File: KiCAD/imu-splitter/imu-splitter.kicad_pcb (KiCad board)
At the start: 4 copper layers, 54 x 54 mm, 11 parts, among them J1 4P4C, J2 4P4C, J3 4P4C, J4 4P4C, J5 4P4C, J6 4P4C, J7 Conn_02x13_Odd_Even, J8 Conn_01x04, U1 AZ1117-3.3

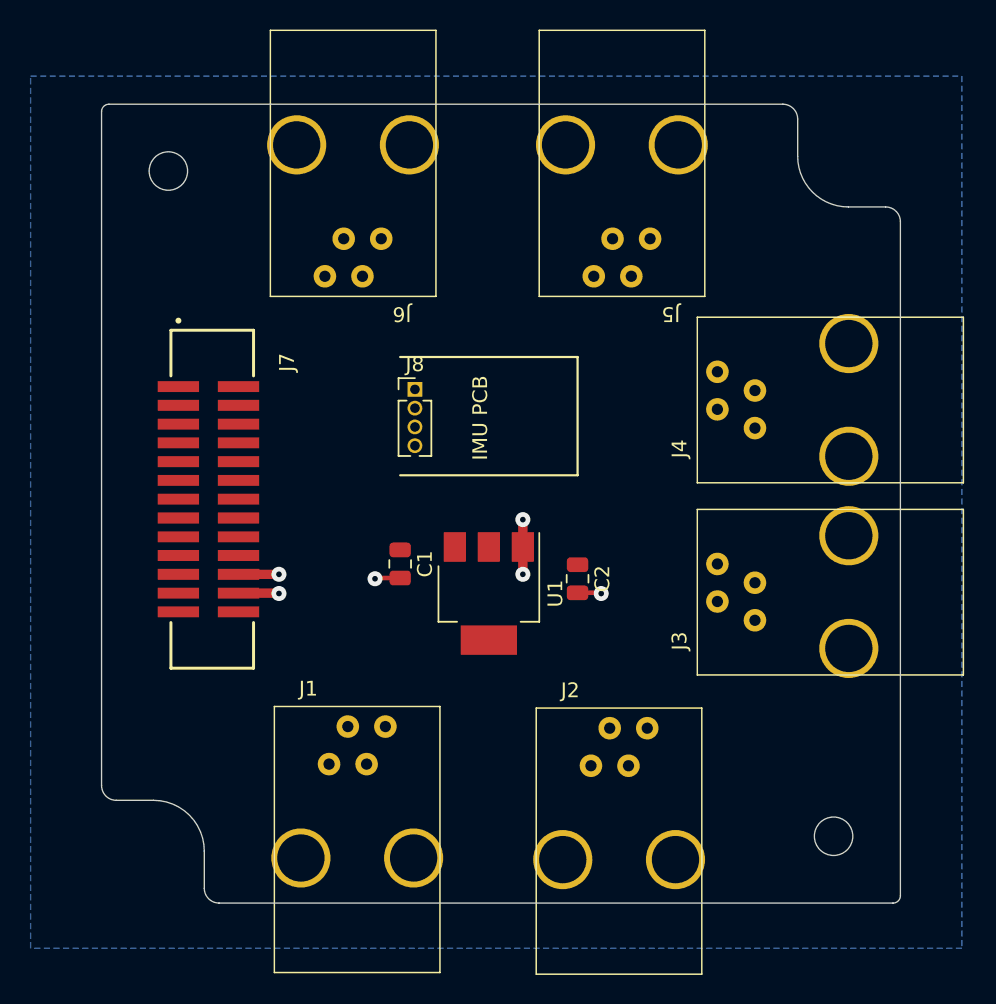
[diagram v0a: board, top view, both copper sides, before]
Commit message: tentative placement of splitter
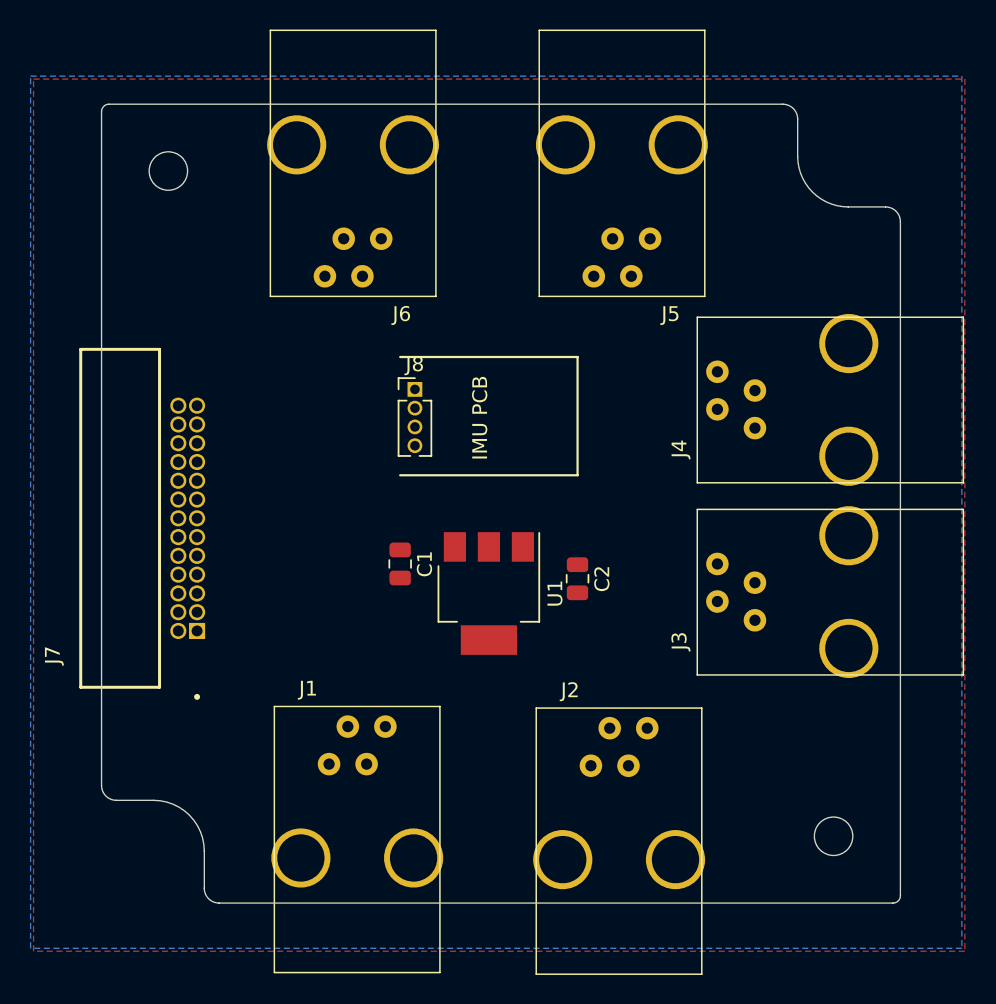
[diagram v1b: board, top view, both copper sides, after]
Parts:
- J7: value Conn_02x13_Odd_Even -> SHF-113-01-L-D-SM; footprint models:SAMTEC_SHF-113-01-L-D-SM -> models:SAMTEC_SHF-113-01-L-D-RA
- moved J7 1.91 mm to (169.6, 102.9), turned to 90 degrees
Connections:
- J2 pad 2: /TX1 -> /RX1
- J2 pad 3: /RX1 -> /TX1
- J7 pad 10: /RX2 -> /TX6
- J7 pad 11: /TX3 -> /TX1
- J7 pad 12: /RX3 -> /RX6
- J7 pad 13: /TX4 -> /RX1
- J7 pad 15: /TX5 -> /TX2
- J7 pad 16: /RX5 -> /TX4
- J7 pad 17: /TX6 -> /RX2
- J7 pad 18: /RX6 -> /RX3
- J7 pad 20: unconnected-(J7-Pin_20-Pad20) -> /TX3
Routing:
- net GND: track 12.5 -> 0.00 mm, vias 6 -> 0
- added copper zone on F.Cu, net +3.3V

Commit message: updates before v1 fab
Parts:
- added D1: LED, LED_SMD:LED_0805_2012Metric_Pad1.15x1.40mm_HandSolder, F.Cu at (183.4, 109.6)
- added D2: LED, LED_SMD:LED_0805_2012Metric_Pad1.15x1.40mm_HandSolder, F.Cu at (197.3, 109.6)
- added J9: Conn_01x05, Connector_PinHeader_2.54mm:PinHeader_1x05_P2.54mm_Vertical, F.Cu at (178.4, 110.1)
- added R1: 1.5k, Resistor_SMD:R_0805_2012Metric_Pad1.20x1.40mm_HandSolder, F.Cu at (182.2, 105.5)
- added R2: 510, Capacitor_SMD:C_0805_2012Metric_Pad1.18x1.45mm_HandSolder, F.Cu at (198.7, 105.6)
- C1, C2: footprint Capacitor_SMD:C_0805_2012Metric -> Capacitor_SMD:C_0805_2012Metric_Pad1.18x1.45mm_HandSolder
- moved C2 1.33 mm to (196.0, 105.7)
- moved C1 0.91 mm to (184.8, 105.5)
- moved J3 0.64 mm to (208.1, 110.4)
- moved J4 0.12 mm to (208.1, 96.8)
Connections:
- J7 pad 10: /TX6 -> /TX1
- J7 pad 11: /TX1 -> /RX6
- J7 pad 12: /RX6 -> /RX1
- J7 pad 13: /RX1 -> /TX6
- J7 pad 14: /RX4 -> /RX0
- J7 pad 15: /TX2 -> /TX4
- J7 pad 16: /TX4 -> /TX0
- J7 pad 17: /RX2 -> /RX4
- J7 pad 18: /RX3 -> unconnected-(J7-Pin_18-Pad18)
- J7 pad 19: unconnected-(J7-Pin_19-Pad19) -> /TX5
- J7 pad 20: /TX3 -> unconnected-(J7-Pin_20-Pad20)
- J7 pad 21: unconnected-(J7-Pin_21-Pad21) -> /RX5
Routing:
- net /RX0: track 0.00 -> 54.2 mm
- net /RX2: track 0.00 -> 48.9 mm
- net /TX2: track 0.00 -> 46.3 mm
- net /TX1: track 0.00 -> 45.6 mm
- net /TX0: track 0.00 -> 45.4 mm
- net /RX1: track 0.00 -> 43.0 mm
- net /RX3: track 0.00 -> 43.0 mm
- net /TX3: track 0.00 -> 40.0 mm
- net /TX4: track 0.00 -> 36.6 mm
- net /RX4: track 0.00 -> 34.9 mm
- net +5V: track 0.00 -> 23.0 mm
- net /RX5: track 0.00 -> 19.6 mm
- net /RX6: track 0.00 -> 17.9 mm
- net /TX6: track 0.00 -> 17.8 mm
- net /TX5: track 0.00 -> 17.2 mm
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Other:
- copper layers 4 -> 2
- board text added: "2024-01 E. Hazen"
- board text added: "3.3"
- board text added: "5.0"
- board text added: "DOSI IMU Splitter V1.0"
- board text added: "GND"
- board text added: "K"
- board text added: "RX0"
- board text added: "TX0"

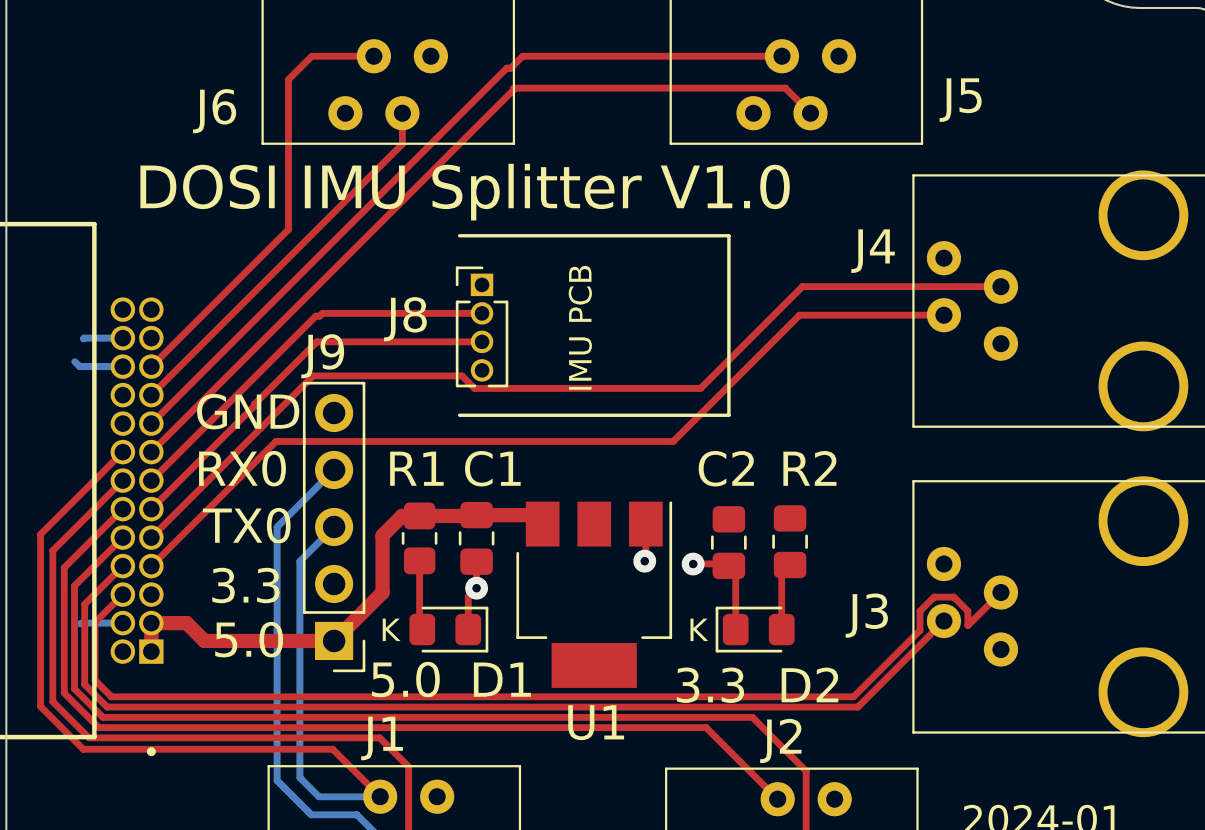
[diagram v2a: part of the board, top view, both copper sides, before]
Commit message: fix silkscreen and move IMU PCB a bit
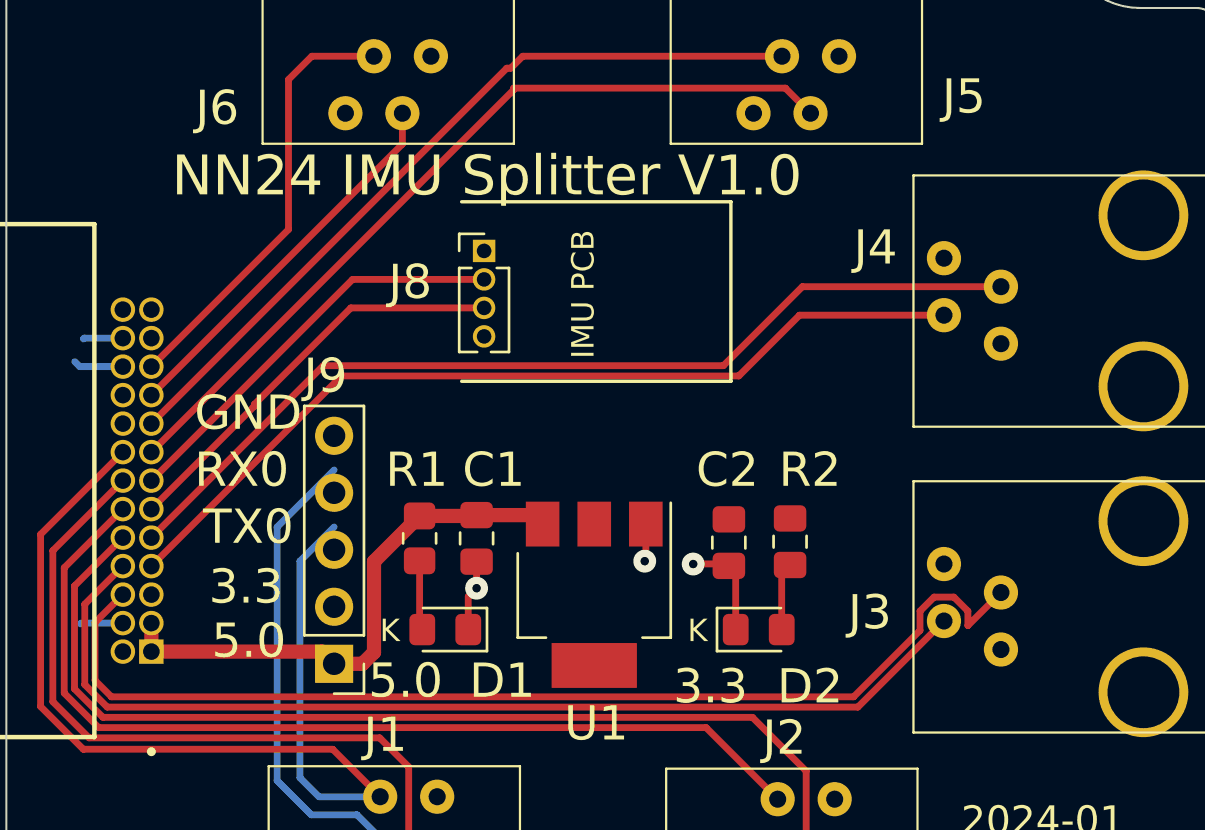
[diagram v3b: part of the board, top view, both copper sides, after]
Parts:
- moved J8 1.52 mm to (185.1, 92.7)
- moved J9 1.02 mm to (178.4, 111.1)
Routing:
- net +5V: track 23.0 -> 24.2 mm
- net /RX6: track 17.9 -> 18.6 mm
- net /TX6: track 17.8 -> 18.5 mm
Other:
- board text added: "NN24 IMU Splitter V1.0"
- board text removed: "DOSI IMU Splitter V1.0"
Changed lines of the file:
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@@
       (drillshape 0)
       (scaleselection 1)
-      (outputdirectory "")
+      (outputdirectory "gerber/")
     )
   )
@@
   )
   (footprint "Connector_PinHeader_1.27mm:PinHeader_1x04_P1.27mm_Vertical" (layer "F.Cu")
-    (at 185 94.19)
+    (at 185.091 92.676)
     (descr "Through hole straight pin header, 1x04, 1.27mm pitch, single row")
     (tags "Through hole pin header THT 1x04 1.27mm single row")
@@
   )
   (footprint "Connector_PinHeader_2.54mm:PinHeader_1x05_P2.54mm_Vertical" (layer "F.Cu")
-    (at 178.407 110.059 180)
+    (at 178.407 111.075 180)
     (descr "Through hole straight pin header, 1x05, 2.54mm pitch, single row")
     (tags "Through hole pin header THT 1x05 2.54mm single row")
@@
     )
   )
-  (gr_line (start 196 100) (end 184 100)
+  (gr_line (start 196.091 98.486) (end 184.091 98.486)
     (stroke (width 0.15) (type default)) (layer "F.SilkS"))
-  (gr_line (start 196 92) (end 196 100)
+  (gr_line (start 196.091 90.486) (end 196.091 98.486)
     (stroke (width 0.15) (type default)) (layer "F.SilkS"))
-  (gr_line (start 184 92) (end 196 92)
+  (gr_line (start 184.091 90.486) (end 196.091 90.486)
     (stroke (width 0.15) (type default)) (layer "F.SilkS"))
   (gr_rect (start 184 92) (end 196 100)
@@
     (effects (font (size 1.524 1.524) (thickness 0.2032)) (justify left bottom))
   )
-  (gr_text "DOSI IMU Splitter V1.0" (at 169.517 91.009) (layer "F.SilkS")
-    (effects (font (size 1.905 1.905) (thickness 0.2032)) (justify left bottom))
+  (gr_text "NN24 IMU Splitter V1.0" (at 171.168 90.374) (layer "F.SilkS")
+    (effects (font (size 1.778 1.778) (thickness 0.2032)) (justify left bottom))
   )
   (gr_text "K" (at 194.155 110.186) (layer "F.SilkS")
     (effects (font (size 1 1) (thickness 0.15)) (justify left bottom))
   )
-  (gr_text "IMU PCB" (at 190 99 90) (layer "F.SilkS")
+  (gr_text "IMU PCB" (at 190.091 97.486 90) (layer "F.SilkS")
     (effects (font (size 1 1) (thickness 0.15)) (justify left bottom))
   )
@@
   )
   (segment (start 184.7195 104.487) (end 184.757 104.4495) (width 0.635) (layer "F.Cu") (net 4))
-  (segment (start 180.566 105.36) (end 181.439 104.487) (width 0.635) (layer "F.Cu") (net 4))
+  (segment (start 180.185 106.519) (end 182.217 104.487) (width 0.635) (layer "F.Cu") (net 4))
+  (segment (start 180.185 110.567) (end 180.185 106.519) (width 0.635) (layer "F.Cu") (net 4))
   (segment (start 184.757 104.4495) (end 187.2995 104.4495) (width 0.635) (layer "F.Cu") (net 4))
-  (segment (start 171.8375 109.2625) (end 172.634 110.059) (width 0.635) (layer "F.Cu") (net 4))
-  (segment (start 172.634 110.059) (end 178.407 110.059) (width 0.635) (layer "F.Cu") (net 4))
+  (segment (start 178.407 111.075) (end 179.677 111.075) (width 0.635) (layer "F.Cu") (net 4))
+  (segment (start 177.8645 110.5325) (end 178.407 111.075) (width 0.635) (layer "F.Cu") (net 4))
   (segment (start 182.217 104.487) (end 184.7195 104.487) (width 0.635) (layer "F.Cu") (net 4))
-  (segment (start 180.566 107.9) (end 180.566 105.36) (width 0.635) (layer "F.Cu") (net 4))
-  (segment (start 170.2625 109.2625) (end 171.8375 109.2625) (width 0.635) (layer "F.Cu") (net 4))
+  (segment (start 170.2625 110.5325) (end 177.8645 110.5325) (width 0.635) (layer "F.Cu") (net 4))
+  (segment (start 179.677 111.075) (end 180.185 110.567) (width 0.635) (layer "F.Cu") (net 4))
   (segment (start 187.2995 104.4495) (end 187.7 104.85) (width 0.635) (layer "F.Cu") (net 4))
-  (segment (start 181.439 104.487) (end 182.217 104.487) (width 0.635) (layer "F.Cu") (net 4))
   (segment (start 170.2625 110.5325) (end 170.2625 109.2625) (width 0.635) (layer "F.Cu") (net 4))
-  (segment (start 178.407 110.059) (end 180.566 107.9) (width 0.635) (layer "F.Cu") (net 4))
   (segment (start 194.414 106.625) (end 194.409 106.63) (width 0.3048) (layer "F.Cu") (net 5))
   (segment (start 192.3 106.453) (end 192.25 106.503) (width 0.3048) (layer "F.Cu") (net 5))
@@
   (segment (start 206.6518 109.3732) (end 206.6518 108.728116) (width 0.3048) (layer "F.Cu") (net 12))
   (segment (start 201.560222 112.5482) (end 168.484934 112.5482) (width 0.3048) (layer "F.Cu") (net 12))
-  (segment (start 170.2625 106.7225) (end 175.816 101.169) (width 0.3048) (layer "F.Cu") (net 13))
-  (segment (start 193.52 101.169) (end 199.149 95.54) (width 0.3048) (layer "F.Cu") (net 13))
+  (segment (start 196.441 98.248) (end 199.149 95.54) (width 0.3048) (layer "F.Cu") (net 13))
   (segment (start 199.149 95.54) (end 205.585 95.54) (width 0.3048) (layer "F.Cu") (net 13))
-  (segment (start 175.816 101.169) (end 193.52 101.169) (width 0.3048) (layer "F.Cu") (net 13))
-  (segment (start 170.2625 105.4525) (end 177.467 98.248) (width 0.3048) (layer "F.Cu") (net 14))
-  (segment (start 184.66664 98.8048) (end 194.7412 98.8048) (width 0.3048) (layer "F.Cu") (net 14))
-  (segment (start 194.7412 98.8048) (end 199.276 94.27) (width 0.3048) (layer "F.Cu") (net 14))
-  (segment (start 177.467 98.248) (end 184.10984 98.248) (width 0.3048) (layer "F.Cu") (net 14))
+  (segment (start 170.2625 106.7225) (end 178.737 98.248) (width 0.3048) (layer "F.Cu") (net 13))
+  (segment (start 178.737 98.248) (end 196.441 98.248) (width 0.3048) (layer "F.Cu") (net 13))
   (segment (start 199.276 94.27) (end 208.125 94.27) (width 0.3048) (layer "F.Cu") (net 14))
-  (segment (start 184.10984 98.248) (end 184.66664 98.8048) (width 0.3048) (layer "F.Cu") (net 14))
+  (segment (start 170.2625 105.4525) (end 177.9242 97.7908) (width 0.3048) (layer "F.Cu") (net 14))
+  (segment (start 195.7552 97.7908) (end 199.276 94.27) (width 0.3048) (layer "F.Cu") (net 14))
+  (segment (start 177.9242 97.7908) (end 195.7552 97.7908) (width 0.3048) (layer "F.Cu") (net 14))
   (segment (start 186.813 84) (end 198.3675 84) (width 0.3048) (layer "F.Cu") (net 15))
   (segment (start 186.281 84.532) (end 186.813 84) (width 0.3048) (layer "F.Cu") (net 15))
@@
   (segment (start 176.375 85.04) (end 177.415 84) (width 0.3048) (layer "F.Cu") (net 18))
   (segment (start 176.375 91.72) (end 176.375 85.04) (width 0.3048) (layer "F.Cu") (net 18))
-  (segment (start 177.772 95.581) (end 177.893 95.46) (width 0.3048) (layer "F.Cu") (net 19))
-  (segment (start 177.594 95.581) (end 177.772 95.581) (width 0.3048) (layer "F.Cu") (net 19))
-  (segment (start 177.893 95.46) (end 185 95.46) (width 0.3048) (layer "F.Cu") (net 19))
-  (segment (start 170.2625 102.9125) (end 177.594 95.581) (width 0.3048) (layer "F.Cu") (net 19))
+  (segment (start 179.229 93.946) (end 185.091 93.946) (width 0.3048) (layer "F.Cu") (net 19))
+  (segment (start 170.2625 102.9125) (end 179.229 93.946) (width 0.3048) (layer "F.Cu") (net 19))
+  (segment (start 179.153 95.216) (end 185.091 95.216) (width 0.3048) (layer "F.Cu") (net 20))
   (segment (start 170.2625 104.1825) (end 174.851 99.594) (width 0.3048) (layer "F.Cu") (net 20))
-  (segment (start 174.851 99.518) (end 177.639 96.73) (width 0.3048) (layer "F.Cu") (net 20))
+  (segment (start 174.851 99.518) (end 179.153 95.216) (width 0.3048) (layer "F.Cu") (net 20))
   (segment (start 174.851 99.594) (end 174.851 99.518) (width 0.3048) (layer "F.Cu") (net 20))
-  (segment (start 177.639 96.73) (end 185 96.73) (width 0.3048) (layer "F.Cu") (net 20))
   (segment (start 182.217 106.487) (end 182.217 109.433) (width 0.3048) (layer "F.Cu") (net 24))
   (segment (start 182.217 109.433) (end 182.335 109.551) (width 0.3048) (layer "F.Cu") (net 24))
